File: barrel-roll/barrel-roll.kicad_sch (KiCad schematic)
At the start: 16 parts, among them M1 Motor_DC, M2 Motor_DC, U1 XIAO-RP2040-DIP, U2 DRV8833PW, U3 WeaponMotor, U4 Recever

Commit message: Worked on the firmware of the bot
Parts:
- MX-5A_ESC1: value ~ -> (none)

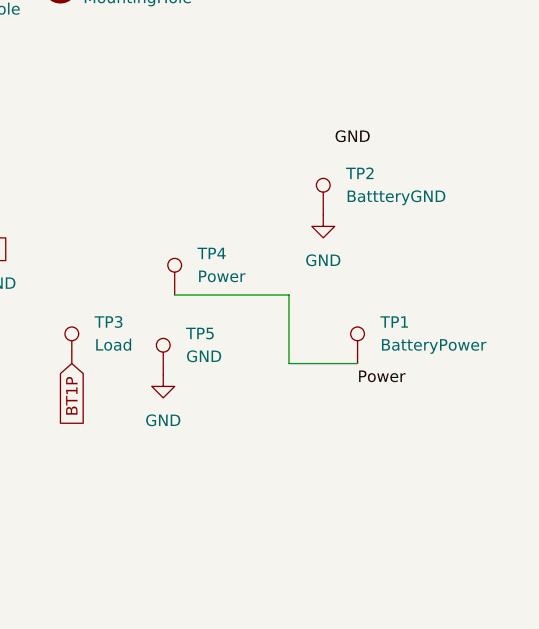
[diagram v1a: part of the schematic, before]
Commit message: Added esp32 support, and worked on the battery conenctor.
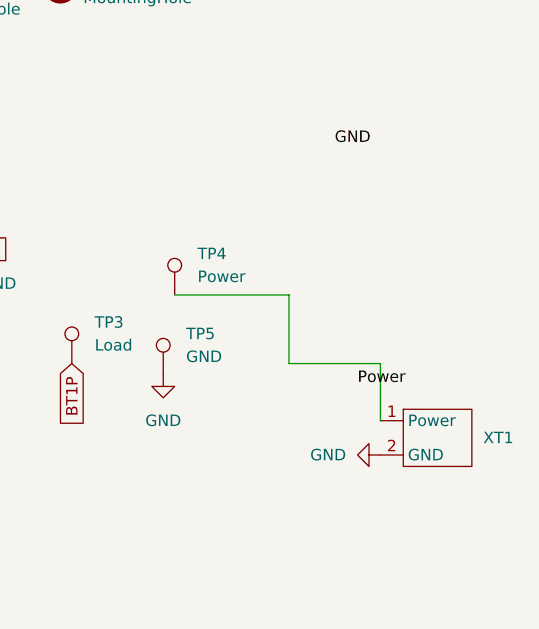
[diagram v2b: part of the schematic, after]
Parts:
- removed TP1: BatteryPower, Connector_Wire:SolderWire-2sqmm_1x01_D2mm_OD3.9mm, symbol Connector:TestPoint
- removed TP2: BattteryGND, Connector_Wire:SolderWire-2sqmm_1x01_D2mm_OD3.9mm, symbol Connector:TestPoint
- added XT1: (no value), Connector_AMASS:AMASS_XT30UPB-F_1x02_P5.0mm_Vertical, symbol New_Library:XT30
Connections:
- net GND: now also XT1.2 (GND)
- net at TP4.1: now also XT1.1 (Power)
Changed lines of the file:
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@@
 	(wire
 		(pts
-			(xy 186.69 102.87) (xy 179.07 102.87)
+			(xy 189.23 102.87) (xy 189.23 109.22)
+		)
+		(stroke
+			(width 0)
+			(type default)
+		)
+	)
+	(wire
+		(pts
+			(xy 179.07 102.87) (xy 189.23 102.87)
 		)
 		(stroke
@@
 	)
 	(symbol
-		(lib_id "Connector:TestPoint")
-		(at 186.69 102.87 0)
-		(unit 1)
-		(body_style 1)
-		(exclude_from_sim no)
-		(in_bom yes)
-		(on_board yes)
-		(in_pos_files yes)
-		(dnp no)
-		(fields_autoplaced yes)
-		(property "Reference" "TP1"
-			(at 189.23 98.2979 0)
-			(show_name no)
-			(do_not_autoplace no)
-			(effects
-				(font
-					(size 1.27 1.27)
-				)
-				(justify left)
-			)
-		)
-		(property "Value" "BatteryPower"
-			(at 189.23 100.8379 0)
-			(show_name no)
-			(do_not_autoplace no)
-			(effects
-				(font
-					(size 1.27 1.27)
-				)
-				(justify left)
-			)
-		)
-		(property "Footprint" "Connector_Wire:SolderWire-2sqmm_1x01_D2mm_OD3.9mm"
-			(at 191.77 102.87 0)
-			(hide yes)
-			(show_name no)
-			(do_not_autoplace no)
-			(effects
-				(font
-					(size 1.27 1.27)
-				)
-			)
-		)
-		(property "Datasheet" ""
-			(at 191.77 102.87 0)
-			(hide yes)
-			(show_name no)
-			(do_not_autoplace no)
-			(effects
-				(font
-					(size 1.27 1.27)
-				)
-			)
-		)
-		(property "Description" "test point"
-			(at 186.69 102.87 0)
-			(hide yes)
-			(show_name no)
-			(do_not_autoplace no)
-			(effects
-				(font
-					(size 1.27 1.27)
-				)
-			)
-		)
-		(pin "1"
-		)
-		(instances
-			(project "barrel-roll"
-				(path "/78e1f998-c6c8-4383-a798-619907ba92a3"
-					(reference "TP1")
-					(unit 1)
-				)
-			)
-		)
-	)
-	(symbol
 		(lib_id "Mechanical:MountingHole")
 		(at 153.67 60.96 0)
@@
 	)
 	(symbol
-		(lib_id "Connector:TestPoint")
-		(at 182.88 86.36 0)
-		(unit 1)
-		(body_style 1)
-		(exclude_from_sim no)
-		(in_bom yes)
-		(on_board yes)
-		(in_pos_files yes)
-		(dnp no)
-		(fields_autoplaced yes)
-		(property "Reference" "TP2"
-			(at 185.42 81.7879 0)
-			(show_name no)
-			(do_not_autoplace no)
-			(effects
-				(font
-					(size 1.27 1.27)
-				)
-				(justify left)
-			)
-		)
-		(property "Value" "BattteryGND"
-			(at 185.42 84.3279 0)
-			(show_name no)
-			(do_not_autoplace no)
-			(effects
-				(font
-					(size 1.27 1.27)
-				)
-				(justify left)
-			)
-		)
-		(property "Footprint" "Connector_Wire:SolderWire-2sqmm_1x01_D2mm_OD3.9mm"
-			(at 187.96 86.36 0)
-			(hide yes)
-			(show_name no)
-			(do_not_autoplace no)
-			(effects
-				(font
-					(size 1.27 1.27)
-				)
-			)
-		)
-		(property "Datasheet" ""
-			(at 187.96 86.36 0)
-			(hide yes)
-			(show_name no)
-			(do_not_autoplace no)
-			(effects
-				(font
-					(size 1.27 1.27)
-				)
-			)
-		)
-		(property "Description" "test point"
-			(at 182.88 86.36 0)
-			(hide yes)
-			(show_name no)
-			(do_not_autoplace no)
-			(effects
-				(font
-					(size 1.27 1.27)
-				)
-			)
-		)
-		(pin "1"
-		)
-		(instances
-			(project "barrel-roll"
-				(path "/78e1f998-c6c8-4383-a798-619907ba92a3"
-					(reference "TP2")
-					(unit 1)
-				)
-			)
-		)
-	)
-	(symbol
 		(lib_id "power:GND")
 		(at 140.97 93.98 90)
@@
 	(symbol
 		(lib_id "power:GND")
-		(at 182.88 86.36 0)
+		(at 189.23 113.03 270)
 		(unit 1)
 		(body_style 1)
@@
 		(dnp no)
 		(fields_autoplaced yes)
-		(property "Reference" "#PWR03"
-			(at 182.88 92.71 0)
+		(property "Reference" "#PWR09"
+			(at 182.88 113.03 0)
 			(hide yes)
 			(show_name no)
@@
 		)
 		(property "Value" "GND"
-			(at 182.88 91.44 0)
-			(show_name no)
-			(do_not_autoplace no)
-			(effects
-				(font
-					(size 1.27 1.27)
-				)
+			(at 185.42 113.0299 90)
+			(show_name no)
+			(do_not_autoplace no)
+			(effects
+				(font
+					(size 1.27 1.27)
+				)
+				(justify right)
 			)
 		)
 		(property "Footprint" ""
-			(at 182.88 86.36 0)
+			(at 189.23 113.03 0)
 			(hide yes)
 			(show_name no)
@@
 		)
 		(property "Datasheet" ""
-			(at 182.88 86.36 0)
+			(at 189.23 113.03 0)
 			(hide yes)
 			(show_name no)
@@
 		)
 		(property "Description" "Power symbol creates a global label with name \"GND\" , ground"
-			(at 182.88 86.36 0)
+			(at 189.23 113.03 0)
 			(hide yes)
 			(show_name no)
@@
 			(project "barrel-roll"
 				(path "/78e1f998-c6c8-4383-a798-619907ba92a3"
-					(reference "#PWR03")
+					(reference "#PWR09")
 					(unit 1)
 				)
@@
 					(unit 1)
 				)
+			)
+		)
+	)
+	(symbol
+		(lib_id "New_Library:XT30")
+		(at 196.85 116.84 0)
+		(unit 1)
+		(body_style 1)
+		(exclude_from_sim no)
+		(in_bom yes)
+		(on_board yes)
+		(in_pos_files yes)
+		(dnp no)
+		(fields_autoplaced yes)
+		(property "Reference" "XT1"
+			(at 200.66 111.1249 0)
+			(show_name no)
+			(do_not_autoplace no)
+			(effects
+				(font
+					(size 1.27 1.27)
+				)
+				(justify left)
+			)
+		)
+		(property "Value" ""
+			(at 196.85 116.84 0)
+			(show_name no)
+			(do_not_autoplace no)
+			(effects
+				(font
+					(size 1.27 1.27)
+				)
+			)
+		)
+		(property "Footprint" "Connector_AMASS:AMASS_XT30UPB-F_1x02_P5.0mm_Vertical"
+			(at 196.85 116.84 0)
+			(hide yes)
+			(show_name no)
+			(do_not_autoplace no)
+			(effects
+				(font
+					(size 1.27 1.27)
+				)
+			)
+		)
+		(property "Datasheet" ""
+			(at 196.85 116.84 0)
+			(hide yes)
+			(show_name no)
+			(do_not_autoplace no)
+			(effects
+				(font
+					(size 1.27 1.27)
+				)
+			)
+		)
+		(property "Description" ""
+			(at 196.85 116.84 0)
+			(hide yes)
+			(show_name no)
+			(do_not_autoplace no)
+			(effects
+				(font
+					(size 1.27 1.27)
+				)
+			)
+		)
+		(pin "1"
+		)
+		(pin "2"
+		)
+		(instances
+			(project "barrel-roll"
+				(path "/78e1f998-c6c8-4383-a798-619907ba92a3"
+					(reference "XT1")
+					(unit 1)
+				)

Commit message: At this point I am really just trying to polish everything up good progress on that though.
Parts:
- removed H1, H2, H3, H4: MountingHole, MountingHole:MountingHole_2.5mm, symbol Mechanical:MountingHole
